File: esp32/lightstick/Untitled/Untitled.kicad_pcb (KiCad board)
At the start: 2 copper layers, 10 parts, among them J1 Conn_02x09_Odd_Even, J2 Conn_01x04_Pin, J3 Conn_01x02_Pin, J4 Conn_01x02_Pin, J5 Conn_01x08_Pin, J6 Conn_01x08_Pin, J7 Conn_01x08_Pin, Q1 S8050

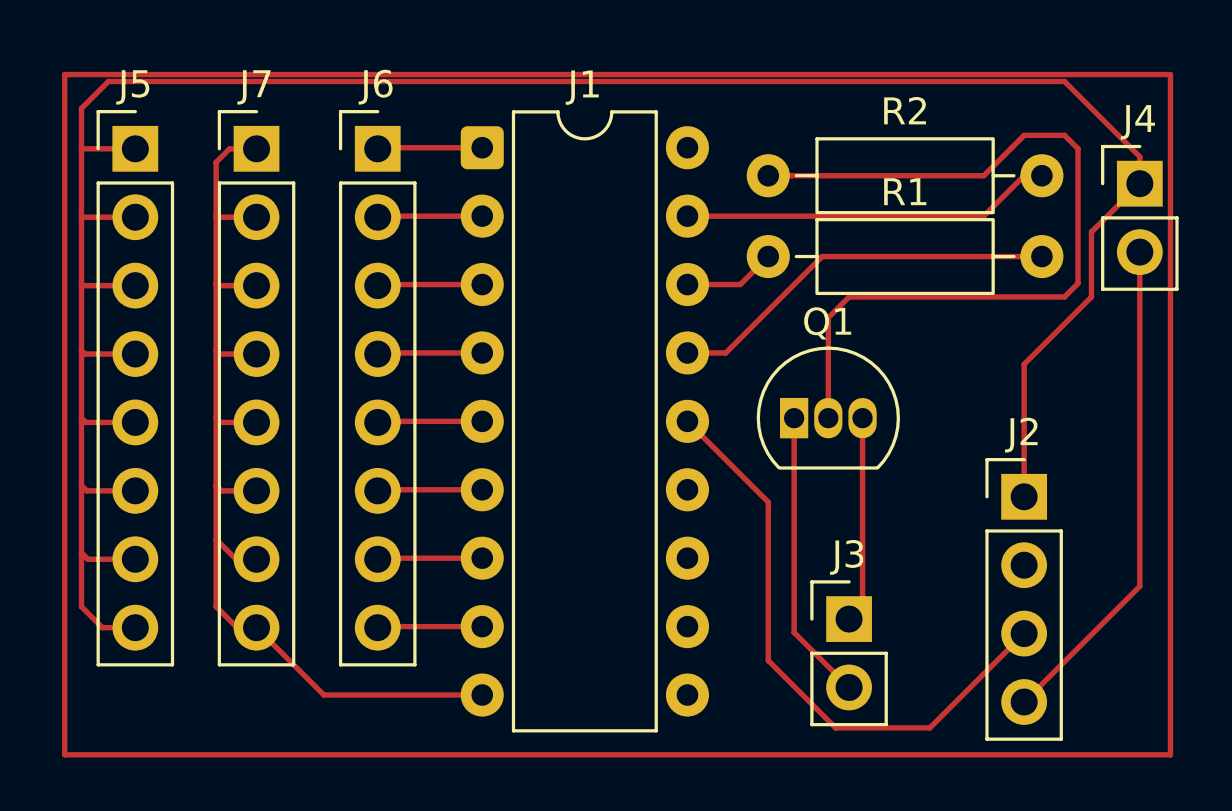
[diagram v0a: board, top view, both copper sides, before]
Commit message: update schematic
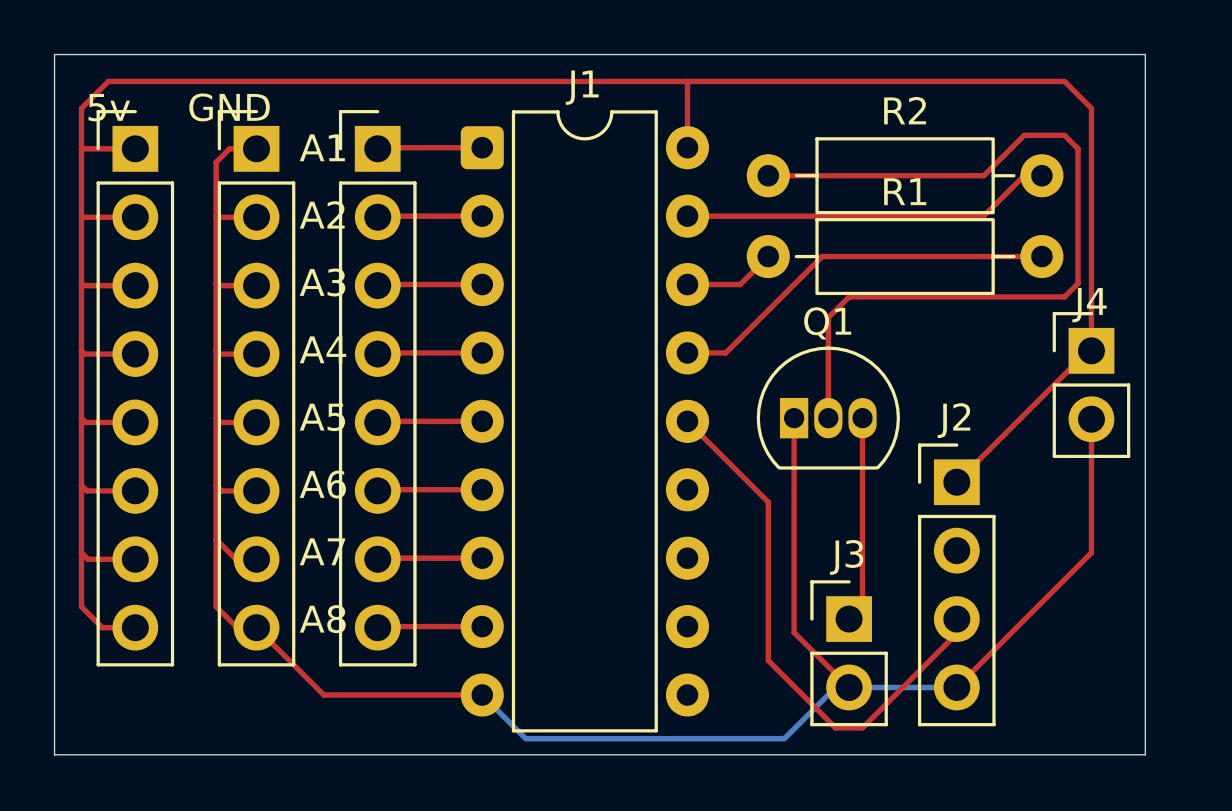
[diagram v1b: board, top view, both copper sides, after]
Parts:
- moved J4 6.46 mm to (133.0, 48.0)
- moved J2 2.56 mm to (128.0, 52.9)
- renumbered J5 to 5v, J6 to A1, J7 to GND
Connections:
- J3 pad 2: Net-(J3-Pin_2) -> GND
- Q1 pad 1: Net-(J3-Pin_2) -> GND
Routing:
- net GND: track 57.5 -> 81.7 mm
- net Net-(J3-Pin_2): track 10.8 -> 0.00 mm
- net Net-(J1-Pin_14): track 22.1 -> 20.1 mm
- net +5V: track 90.4 -> 92.1 mm
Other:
- board outline added: 40.5 x 26 mm
- board text added: "A2"
- board text added: "A3"
- board text added: "A4"
- board text added: "A5"
- board text added: "A6"
- board text added: "A7"
- board text added: "A8"
